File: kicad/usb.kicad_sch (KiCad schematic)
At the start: 40 parts, among them J14 HX PZ2.54-2X5P TP, U11 TPD4EUSB30DQAR-N, U2 TPD4EUSB30DQAR-N, U3 FSUSB42MUX, U4 USB2514B-I/M2, U5 AP22653W6-7, U6 TPD4EUSB30DQAR-N, X1 X322524MOB4SI

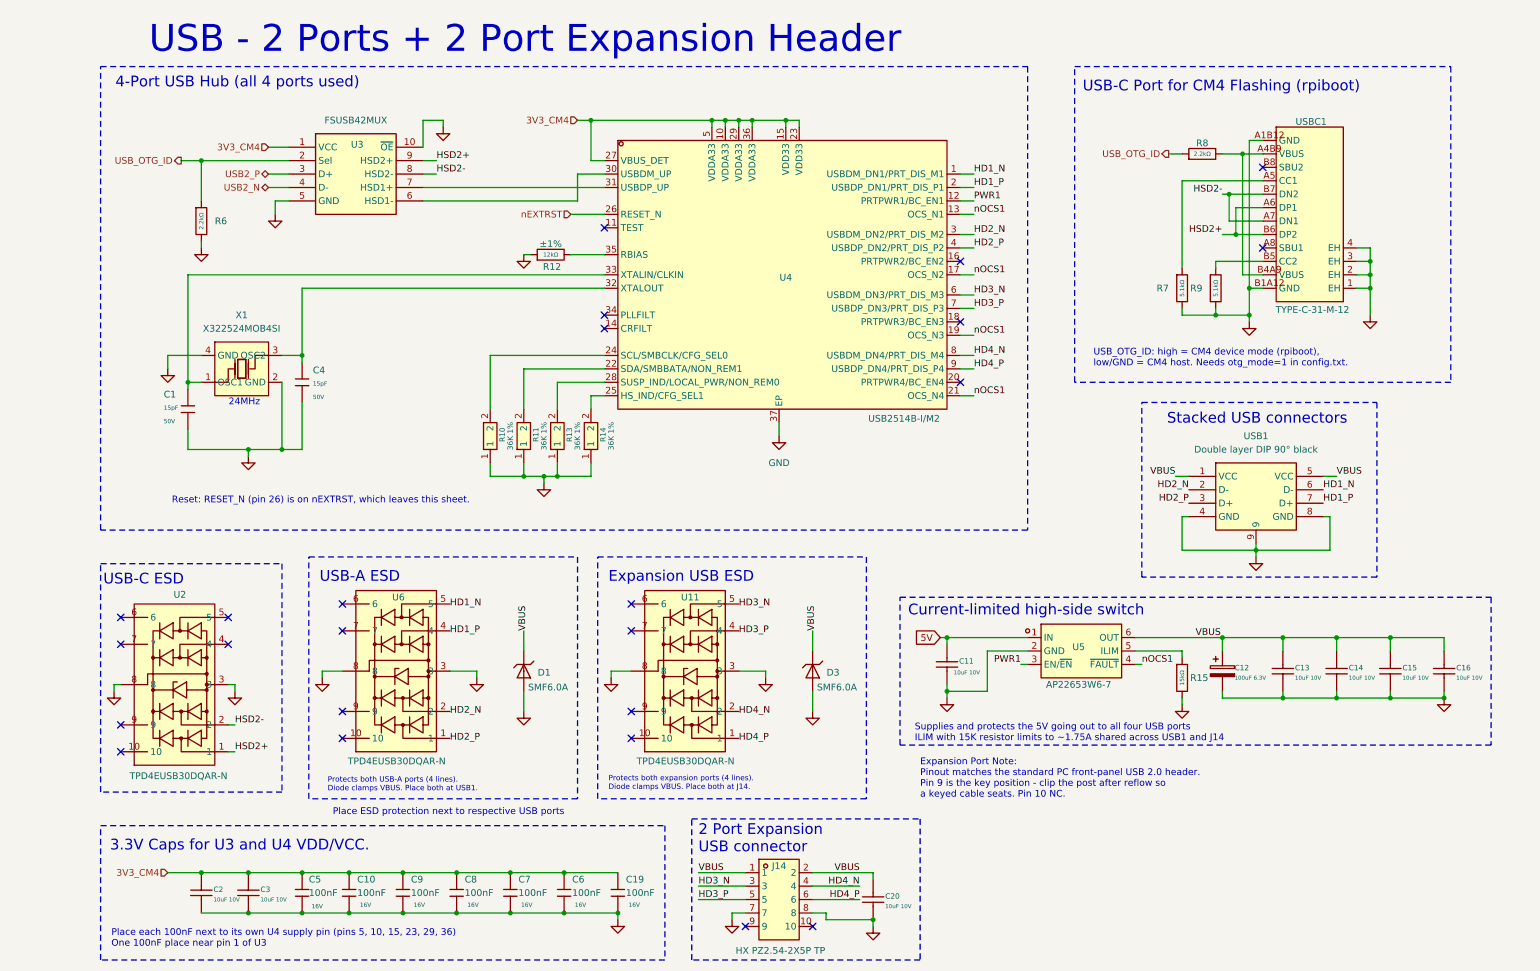
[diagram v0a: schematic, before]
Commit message: GPIO connectors defined
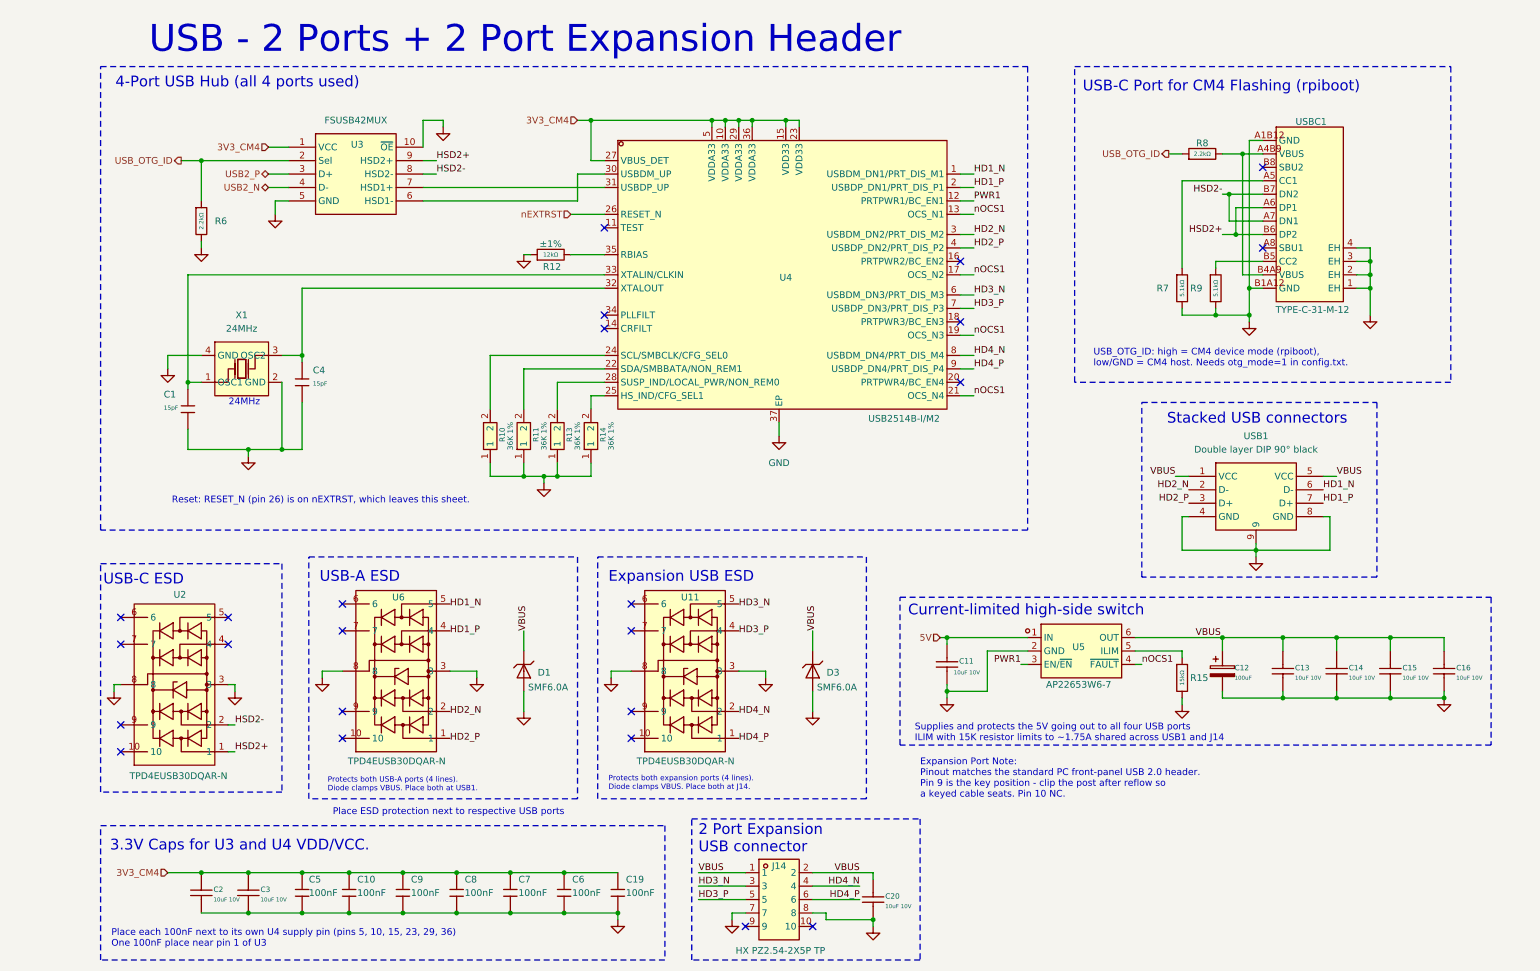
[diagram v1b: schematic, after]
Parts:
- C1, C4: footprint PCM_JLCPCB:C_0402 -> MyParts:C0402; symbol PCM_JLCPCB-Capacitors:0402,15pF -> MyParts:0402CG150J500NT; Attrition Qty 10 -> (none); Capacitance 15pF -> (none); Category Capacitors,Multilayer Ceramic Capacitors MLCC - SMD/SMT -> (none); Class Basic Component -> (none); LCSC C1548 -> (none); LCSC Part (none) -> C1548; MPN (none) -> 0402CG150J500NT; Manufacturer FH(Guangdong Fenghua Advanced Tech) -> FH; Minimum Qty 20 -> (none); Part 0402CG150J500NT -> (none); Price 0.004USD -> (none); Process SMT -> (none); Stock 959507 -> (none); Temperature Coefficient C0G -> (none); Voltage Rated 50V -> (none); Voltage Rating (none) -> 50V
- C10, C19, C5, C6, C7, C8, C9: footprint PCM_JLCPCB:C_0402 -> MyParts:C0402; symbol PCM_JLCPCB-Capacitors:0402,100nF -> MyParts:CL05B104KO5NNNC_ALT; Attrition Qty 10 -> (none); Capacitance 100nF -> (none); Category Capacitors,Multilayer Ceramic Capacitors MLCC - SMD/SMT -> (none); Class Basic Component -> (none); LCSC C1525 -> (none); LCSC Part (none) -> C1525; MPN (none) -> CL05B104KO5NNNC; Manufacturer Samsung Electro-Mechanics -> SAMSUNG; Minimum Qty 20 -> (none); Part CL05B104KO5NNNC -> (none); Price 0.004USD -> (none); Process SMT -> (none); Stock 20208285 -> (none); Temperature Coefficient X7R -> (none); Voltage Rated 16V -> (none); Voltage Rating (none) -> 16V
- C11, C13, C14, C15, C16, C2, C20, C3: Manufacturer SAMSUNG(三星) -> SAMSUNG; Tolerance (none) -> ±10%; Voltage Rating (none) -> 10V
- C12: value 100uF 6.3V -> 100uF; symbol Device:C_Polarized -> MyParts:EEFCX0J101R; Tolerance (none) -> ±20%; Voltage Rating (none) -> 6.3V
- D1, D3: symbol PCM_JLCPCB-Diodes:TVS-Uni,SMF6.0A -> MyParts:SMF6.0A; Attrition Qty 4 -> (none); Category Circuit Protection,ESD And Surge Protection (TVS/ESD) -> (none); Class Preferred Component -> (none); LCSC C19077499 -> (none); LCSC Part (none) -> C19077499; MPN (none) -> SMF6.0A; Minimum Qty 15 -> (none); Part SMF6.0A -> (none); Price 0.029USD -> (none); Process SMT -> (none); Stock 42202 -> (none)
- J14: Manufacturer hanxia(韩下) -> hanxia
- R10, R11, R13, R14: Manufacturer FOJAN(富捷) -> FOJAN; Tolerance (none) -> ±1%; Voltage Rating (none) -> 50V
- R12: symbol PCM_JLCPCB-Resistors:0402,12kΩ -> MyParts:0402WGF1202TCE; Attrition Qty 10 -> (none); Category Resistors,Chip Resistor - Surface Mount -> (none); Class Basic Component -> (none); LCSC C25752 -> (none); LCSC Part (none) -> C25752; MPN (none) -> 0402WGF1202TCE; Manufacturer UNI-ROYAL(Uniroyal Elec) -> UNI-ROYAL; Minimum Qty 20 -> (none); Operating Temperature Range -55°C~+155°C -> (none); Overload Voltage (Max) 50V -> (none); Part 0402WGF1202TCE -> (none); Power(Watts) 62.5mW -> (none); Price 0.004USD -> (none); Process SMT -> (none); Resistance 12kΩ -> (none); Stock 342039 -> (none); Temperature Coefficient ±100ppm/°C -> (none); Type Thick Film Resistors -> (none); Voltage Rating (none) -> 50V
- R15: footprint PCM_JLCPCB:R_0402 -> MyParts:R0402; symbol PCM_JLCPCB-Resistors:0402,15kΩ -> MyParts:0402WGF1502TCE; Attrition Qty 10 -> (none); Category Resistors,Chip Resistor - Surface Mount -> (none); Class Basic Component -> (none); LCSC C25756 -> (none); LCSC Part (none) -> C25756; MPN (none) -> 0402WGF1502TCE; Manufacturer UNI-ROYAL(Uniroyal Elec) -> UNI-ROYAL; Minimum Qty 20 -> (none); Operating Temperature Range -55°C~+155°C -> (none); Overload Voltage (Max) 50V -> (none); Part 0402WGF1502TCE -> (none); Power(Watts) 62.5mW -> (none); Price 0.004USD -> (none); Process SMT -> (none); Resistance 15kΩ -> (none); Stock 671055 -> (none); Temperature Coefficient ±100ppm/°C -> (none); Type Thick Film Resistors -> (none); Voltage Rating (none) -> 50V
- R6, R8: symbol PCM_JLCPCB-Resistors:0402,2.2kΩ -> MyParts:0402WGF2201TCE; Attrition Qty 10 -> (none); Category Resistors,Chip Resistor - Surface Mount -> (none); Class Basic Component -> (none); LCSC C25879 -> (none); LCSC Part (none) -> C25879; MPN (none) -> 0402WGF2201TCE; Manufacturer UNI-ROYAL(Uniroyal Elec) -> UNI-ROYAL; Minimum Qty 20 -> (none); Operating Temperature Range -55°C~+155°C -> (none); Overload Voltage (Max) 50V -> (none); Part 0402WGF2201TCE -> (none); Power(Watts) 62.5mW -> (none); Price 0.004USD -> (none); Process SMT -> (none); Resistance 2.2kΩ -> (none); Stock 1767502 -> (none); Temperature Coefficient ±100ppm/°C -> (none); Type Thick Film Resistors -> (none); Voltage Rating (none) -> 50V
- R7, R9: footprint PCM_JLCPCB:R_0402 -> MyParts:R0402; symbol PCM_JLCPCB-Resistors:0402,5.1kΩ -> MyParts:0402WGF5101TCE; Attrition Qty 10 -> (none); Category Resistors,Chip Resistor - Surface Mount -> (none); Class Basic Component -> (none); LCSC C25905 -> (none); LCSC Part (none) -> C25905; MPN (none) -> 0402WGF5101TCE; Manufacturer UNI-ROYAL(Uniroyal Elec) -> UNI-ROYAL; Minimum Qty 20 -> (none); Operating Temperature Range -55°C~+155°C -> (none); Overload Voltage (Max) 50V -> (none); Part 0402WGF5101TCE -> (none); Power(Watts) 62.5mW -> (none); Price 0.004USD -> (none); Process SMT -> (none); Resistance 5.1kΩ -> (none); Stock 3534773 -> (none); Temperature Coefficient ±100ppm/°C -> (none); Type Thick Film Resistors -> (none); Voltage Rating (none) -> 50V
- U11, U2, U6: Manufacturer BORN(伯恩半导体) -> BORN
- U3: Manufacturer onsemi(安森美) -> onsemi
- U4: Manufacturer MICROCHIP(美国微芯) -> MICROCHIP
- U5: Manufacturer DIODES(美台) -> DIODES
- USB1: Manufacturer 精拓金 -> Jing Extension of the Electronic Co.
- USBC1: Manufacturer 韩国韩荣 -> Korean Hroparts Elec
- X1: value X322524MOB4SI -> 24MHz; Frequency (none) -> 24MHz; Frequency Stability (none) -> ±20ppm; Frequency Tolerance (none) -> ±10ppm; Load Capacitance (none) -> 12pF; Manufacturer YXC(扬兴晶振) -> YXC

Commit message: schematic cleanup
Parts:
- added R135: 10kΩ, MyParts:R0402, symbol MyParts:0402WGF1002TCE
- added TP20, TP21, TP23: TestPoint_Small, TestPoint:TestPoint_Pad_D1.5mm, symbol Connector:TestPoint_Small
- C11, C13, C14, C15, C16, C2, C20, C3: value 10uF 10V -> 10uF
- R10, R11, R13, R14: value 36K 1% -> 36kΩ
- U11, U2, U6: value TPD4EUSB30DQAR-N -> TPD4EUSB30DQAR; footprint MyParts:DFN-10_L2.5-W1.0-P0.50-BL-A -> MyParts:USON-10_L2.5-W1.0-P0.50-BL; symbol MyParts:TPD4EUSB30DQAR-N -> MyParts:TPD4EUSB30DQAR; LCSC Part C5148477 -> C90627; MPN TPD4EUSB30DQAR-N -> TPD4EUSB30DQAR; Manufacturer BORN -> TI
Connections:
- net 3V3_CM4: now also R135.1
- net GND: now also TP23.1
- net nOCS1: now also R135.2
- net at R8.2, USBC1.A4B9 (VBUS), USBC1.B4A9 (VBUS): now also TP20.1
- net USB_HUB_N: now reaches U3.6 (HSD1-), U4.30 (USBDM_UP)
- net USB_HUB_P: now reaches U3.7 (HSD1+), U4.31 (USBDP_UP)
- net Net-(U5-ILIM): now reaches R15.1, U5.5 (ILIM)
- net Net-(U5-ILIM): now also TP21.1
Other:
- note added: "USB_OTG_ID: high = CM4 device mode (rpiboot), low/GND = CM4 host. Needs otg_mode=1 in config.txt. USBC1 VBUS: 5.0 V nom (4.75 V min / 5.5 V max). No USB-PD controller; CC has 5.1 kΩ Rd only. VBUS used only for detect: R8/R6 divider -> USB_OTG_ID (2.75 V max)."
- note removed: "USB_OTG_ID: high = CM4 device mode (rpiboot), low/GND = CM4 host. Needs otg_mode=1 in config.txt."
- moved on the sheet: D1, D3, USB1

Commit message: Still refining
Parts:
- C1, C10, C19, C4, C5, C6, C7, C8, C9, R10, R11, R12, R13, R135, R14, R15, R6, R7, R8, R9: Pkg Type (none) -> SMD 0402
- C11, C13, C14, C15, C16, C2, C20, C3: Pkg Type (none) -> SMD 0805
- C12: Pkg Type (none) -> SMD EIA-7343 (D case)
- D1, D3: Pkg Type (none) -> SMD SOD-123FL
- J14: Pkg Type (none) -> SMD Pin header 2x5 P2.54
- TP20, TP21, TP23: Pkg Type (none) -> SMD Test pad D1.5
- U11, U2, U6: Pkg Type (none) -> SMD USON-10 2.5x1.0
- U3: Pkg Type (none) -> SMD MSOP-10
- U4: Pkg Type (none) -> SMD QFN-36 6.0x6.0 EP
- U5: Pkg Type (none) -> SMD SOT-23-6
- USB1: Pkg Type (none) -> THT USB-A dual stacked
- USBC1: Pkg Type (none) -> SMD+THT USB-C receptacle
- X1: Pkg Type (none) -> SMD Crystal 3225 4-pad
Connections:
- net GND: no longer USB1.9, USBC1.1 (EH), USBC1.2 (EH), USBC1.3 (EH), USBC1.4 (EH)
- new net CHASSIS: USB1.9, USBC1.1 (EH), USBC1.2 (EH), USBC1.3 (EH), USBC1.4 (EH)
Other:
- note added: "USB_OTG_ID: high = CM4 device mode (rpiboot), low/GND = CM4 host. Needs otg_mode=1 in config.txt. USBC1 VBUS: 5.0 V nom (4.75 V min / 5.5 V max). No USB-PD controller; CC has 5.1 kΩ Rd only. VBUS used only for detect: R8/R6 divider -> USB_OTG_ID (2.75 V max). VBUS current: 1.25 mA continuous / 1.25 mA peak. VBUS survives up to 6.6 V, down to -1.0 V."
- note removed: "USB_OTG_ID: high = CM4 device mode (rpiboot), low/GND = CM4 host. Needs otg_mode=1 in config.txt. USBC1 VBUS: 5.0 V nom (4.75 V min / 5.5 V max). No USB-PD controller; CC has 5.1 kΩ Rd only. VBUS used only for detect: R8/R6 divider -> USB_OTG_ID (2.75 V max)."

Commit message: Mods
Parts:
- removed R6, R8: 2.2kΩ, MyParts:R0402, symbol MyParts:0402WGF2201TCE
- removed R7, R9: 5.1kΩ, MyParts:R0402, symbol MyParts:0402WGF5101TCE
- removed TP20: TestPoint_Small, TestPoint:TestPoint_Pad_D1.5mm, symbol Connector:TestPoint_Small
- removed USBC1: TYPE-C-31-M-12, MyParts:USB-C_SMD-TYPE-C-31-M-12_1, symbol MyParts:TYPE-C-31-M-12
- added C111, C112: 100nF, MyParts:C0402, symbol MyParts:CL05B104KO5NNNC_ALT
- added D52, D53: BAT54C, MyParts:SOT-23-3_L2.9-W1.6-P1.90-LS2.8-BR, symbol MyParts:BAT54C
- added R138: 100kΩ, MyParts:R0603, symbol MyParts:0603WAF1003T5E
- added TP31: TestPoint_Small, TestPoint:TestPoint_Pad_D1.5mm, symbol Connector:TestPoint_Small
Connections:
- net 3V3_CM4: now also R135.2; no longer R135.1
- net 5V: now also C112.1
- net GND: now also C111.2, C112.2, R138.2, TP31.1
- net PWR1: now also D52.1 (A); no longer U5.3 (EN/~{EN})
- net VBUS: now also C111.1
- net nOCS1: now also R135.1; no longer R135.2
- net PWR2: now reaches U4.16 (PRTPWR2/BC_EN2)
- net PWR2: now also D52.2 (A)
- net PWR3: now reaches U4.18 (PRTPWR3/BC_EN3)
- net PWR3: now also D53.1 (A)
- net PWR4: now reaches U4.20 (PRTPWR4/BC_EN4)
- net PWR4: now also D53.2 (A)
- new net U5_EN: D52.3 (K), D53.3 (K), R138.1, U5.3 (EN/~{EN})
- no-connect marks 24 -> 19
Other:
- added sheet usb2 (usb2.kicad_sch)
- note added: "U5 port power, diode-OR (D52/D53, R138). The hub straps CFG_SEL=00: individual port power switching and OC sensing (USB2514B Table 5-1). U5 feeds all four ports, so its EN is the OR of PRTPWR1-4: VBUS stays on while any port is enabled and drops only when all four are off. OCS_N1-4 share nOCS1: a U5 fault is reported on every port (correct for one shared switch). BC_EN straps read 0 via the inter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"
- note removed: "USB-C Port for CM4 Flashing (rpiboot)"
- note removed: "USB_OTG_ID: high = CM4 device mode (rpiboot), low/GND = CM4 host. Needs otg_mode=1 in config.txt. USBC1 VBUS: 5.0 V nom (4.75 V min / 5.5 V max). No USB-PD controller; CC has 5.1 kΩ Rd only. VBUS used only for detect: R8/R6 divider -> USB_OTG_ID (2.75 V max). VBUS current: 1.25 mA continuous / 1.25 mA peak. VBUS survives up to 6.6 V, down to -1.0 V."
- moved on the sheet: C1, C4, R10, R11, R12, R13, R135, R14, TP21, U3, U4, USB1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

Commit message: Ready to start layout
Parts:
- renumbered C14 to C10, C15 to C11, C16 to C12, C2 to C13, C3 to C14, C5 to C15, C10 to C16, C9 to C17, C8 to C18, C7 to C19, C6 to C20, C19 to C21, C20 to C22, C4 to C3, C1 to C4, C11 to C5, C112 to C6, C12 to C7, C111 to C8, C13 to C9, D52 to D6, D53 to D7, D1 to D8, D3 to D9, J14 to J2, R12 to R10, R138 to R11, R10 to R12, R11 to R13, R13 to R14, R14 to R15, R135 to R16, R15 to R17, TP23 to TP10, TP31 to TP8, TP21 to TP9, U3 to U2, U4 to U3, U5 to U4, U2 to U5, U11 to U7
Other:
- note added: "3.3V Caps for U2 and U3 VDD/VCC."
- note added: "Place each 100nF next to its own U3 supply pin (pins 5, 10, 15, 23, 29, 36) One 100nF place near pin 1 of U2"
- note added: "Protects both expansion ports (4 lines). Diode clamps VBUS. Place both at J2."
- note added: "Supplies and protects the 5V going out to all four USB ports ILIM with 15K resistor limits to ~1.75A shared across USB1 and J2"
- note added: "U4 port power, diode-OR (D6/D7, R11). The hub straps CFG_SEL=00: individual port power switching and OC sensing (USB2514B Table 5-1). U4 feeds all four ports, so its EN is the OR of PRTPWR1-4: VBUS stays on while any port is enabled and drops only when all four are off. OCS_N1-4 share nOCS1: a U4 fault is reported on every port (correct for one shared switch). BC_EN straps read 0 via the internal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"
- note removed: "3.3V Caps for U3 and U4 VDD/VCC."
- note removed: "Place each 100nF next to its own U4 supply pin (pins 5, 10, 15, 23, 29, 36) One 100nF place near pin 1 of U3"
- note removed: "Protects both expansion ports (4 lines). Diode clamps VBUS. Place both at J14."
- note removed: "Supplies and protects the 5V going out to all four USB ports ILIM with 15K resistor limits to ~1.75A shared across USB1 and J14"
- note removed: "U5 port power, diode-OR (D52/D53, R138). The hub straps CFG_SEL=00: individual port power switching and OC sensing (USB2514B Table 5-1). U5 feeds all four ports, so its EN is the OR of PRTPWR1-4: VBUS stays on while any port is enabled and drops only when all four are off. OCS_N1-4 share nOCS1: a U5 fault is reported on every port (correct for one shared switch). BC_EN straps read 0 via the inter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"

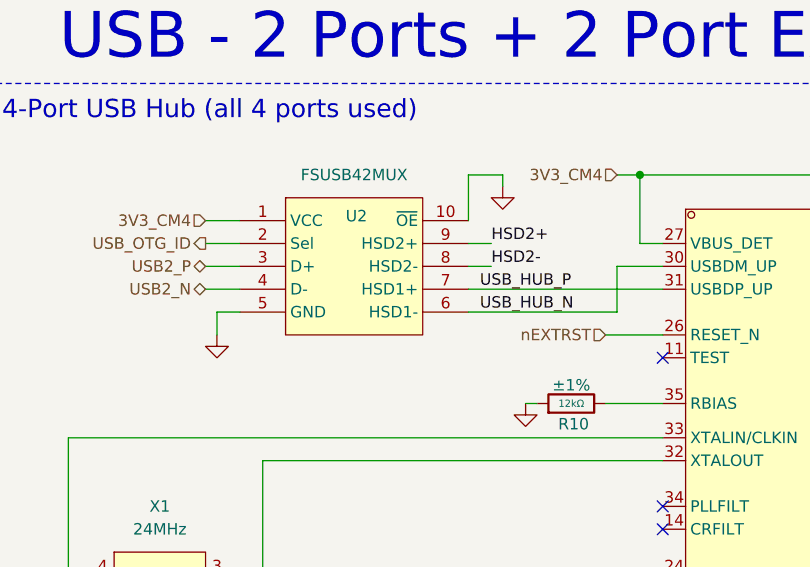
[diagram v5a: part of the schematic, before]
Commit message: IPC footprint renaming, battery sim added
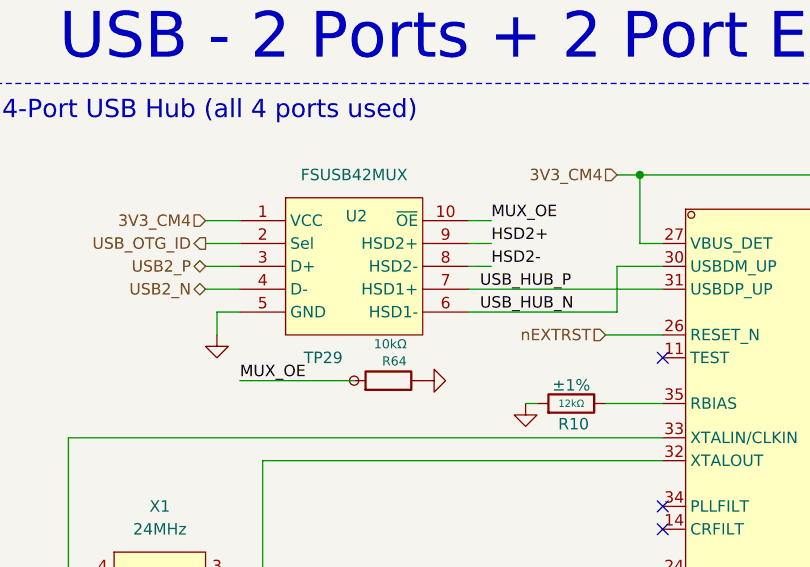
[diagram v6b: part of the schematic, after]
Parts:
- added R64: 10kΩ, MyPartsIPC:RESC1005X40N, symbol MyParts:0402WGF1002TCE
- added TP29: TestPoint_Small, TestPoint:TestPoint_Pad_D1.5mm, symbol Connector:TestPoint_Small
- C10, C11, C12, C13, C14, C22, C5, C9: footprint MyParts:C0805 -> MyPartsIPC:CAPC2012X145N
- C15, C16, C17, C18, C19, C20, C21, C3, C4, C6, C8: footprint MyParts:C0402 -> MyPartsIPC:CAPC1005X55N
- C7: footprint Capacitor_Tantalum_SMD:CP_EIA-7343-31_Kemet-D -> MyPartsIPC:CAPMP7343X310N
- D6, D7: footprint MyParts:SOT-23-3_L2.9-W1.6-P1.90-LS2.8-BR -> MyPartsIPC:SOT95P280X110-3N
- D8, D9: footprint PCM_JLCPCB:D_SOD-123FL -> MyPartsIPC:SODFL3718X110N
- R10, R12, R13, R14, R15, R16, R17: footprint MyParts:R0402 -> MyPartsIPC:RESC1005X40N
- R11: footprint MyParts:R0603 -> MyPartsIPC:RESC1608X55N
- TP8: now left out of the parts list
- U2: footprint MyParts:MSOP-10_L3.0-W3.0-P0.50-LS5.0-BL -> MyPartsIPC:SOP50P500X110-10N
- U3: footprint MyParts:SQFN-36_L6.0-W6.0-P0.50-BL-EP -> MyPartsIPC:QFN50P600X600X100-37N
- U4: footprint MyParts:SOT-23-6_L2.9-W1.6-P0.95-LS2.8-BR -> MyPartsIPC:SOT95P280X145-6N
- U5, U6, U7: footprint MyParts:USON-10_L2.5-W1.0-P0.50-BL -> MyPartsIPC:SON50P100X250X60-10N
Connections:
- net GND: now also R64.2; no longer U2.10 (~{OE})
- new net MUX_OE: R64.1, TP29.1, U2.10 (~{OE})
